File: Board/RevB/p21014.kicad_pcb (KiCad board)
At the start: 2 copper layers, 53.3 x 25.4 mm, 1 part

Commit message: Roughed out RevB PCB layout
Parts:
- added BT1: Battery_Cell, 0_MSD_FPs:AJS-Coin-Cell_1027-Digikey, B.Cu at (222.2, 60.2)
- added C1: 0.1uF, Capacitor_SMD:C_0603_1608Metric, F.Cu at (159.3, 44.6)
- added C2: 1uF, Capacitor_SMD:C_0603_1608Metric, F.Cu at (159.3, 42.1)
- added C3: 1uF, Capacitor_SMD:C_0603_1608Metric, F.Cu at (155.3, 44.6)
- added C4: 1uF, Capacitor_SMD:C_0603_1608Metric, F.Cu at (155.3, 42.1)
- added C5: 4.7uF_16V, Capacitor_Tantalum_SMD:CP_EIA-3216-18_Kemet-A, F.Cu at (156.2, 39.3)
- added D1: LED_RGB, 0_MSD_FPs:RGB_AJS, F.Cu at (128.6, 38.6)
- added D2: LED, LED_SMD:LED_1812_4532Metric, F.Cu at (118.2, 49.6)
- added J1: Conn_01x06_Male, 0_MSD_FPs:MSD_6_Pin, B.Cu at (193.7, 70.3)
- added J3: Conn_02x03_Counter_Clockwise, Connector_PinHeader_2.54mm:PinHeader_2x03_P2.54mm_Vertical, F.Cu at (214.0, 57.6)
- added J4: Conn_01x08_Female, 0_MSD_FPs:MSD_8_Pin, F.Cu at (179.8, 70.3)
- added J5: Conn_01x12_Female, 0_MSD_FPs:MSD_12_Pin, F.Cu at (190.0, 50.0)
- added J6: Conn_01x06_Female, 0_MSD_FPs:MSD_6_Pin, F.Cu at (205.2, 70.3)
- added MH1: MountingHole_2.5mm, MountingHole:MountingHole_2.5mm, F.Cu at (176.0, 51.3)
- added MH2: MountingHole_2.5mm, MountingHole:MountingHole_2.5mm, F.Cu at (224.3, 51.3)
- added MH3: MountingHole_2.5mm, MountingHole:MountingHole_2.5mm, F.Cu at (176.0, 69.0)
- added MH4: MountingHole_2.5mm, MountingHole:MountingHole_2.5mm, F.Cu at (224.3, 69.0)
- added R1: 350, Resistor_SMD:R_0603_1608Metric, F.Cu at (121.7, 41.4)
- added R2: 350, Resistor_SMD:R_0603_1608Metric, F.Cu at (125.7, 38.9)
- added R3: 350, Resistor_SMD:R_0603_1608Metric, F.Cu at (116.7, 53.3)
- added R4: 350, Resistor_SMD:R_0603_1608Metric, F.Cu at (121.7, 38.9)
- added R5: 10k, Resistor_SMD:R_0603_1608Metric, F.Cu at (123.7, 44.0)
- added R6: 10k, Resistor_SMD:R_0603_1608Metric, F.Cu at (125.7, 41.4)
- added R7: 10k, Resistor_SMD:R_0603_1608Metric, F.Cu at (109.8, 82.1)
- added SW1: SW_Push, 0_MSD_FPs:AJS-Switch_CFS-0102TA, B.Cu at (198.1, 31.8)
- added VR1: LM1117IMPX-5.0, LM1117IMPX-5:SOT230P700X180-4N, F.Cu at (148.5, 41.7)

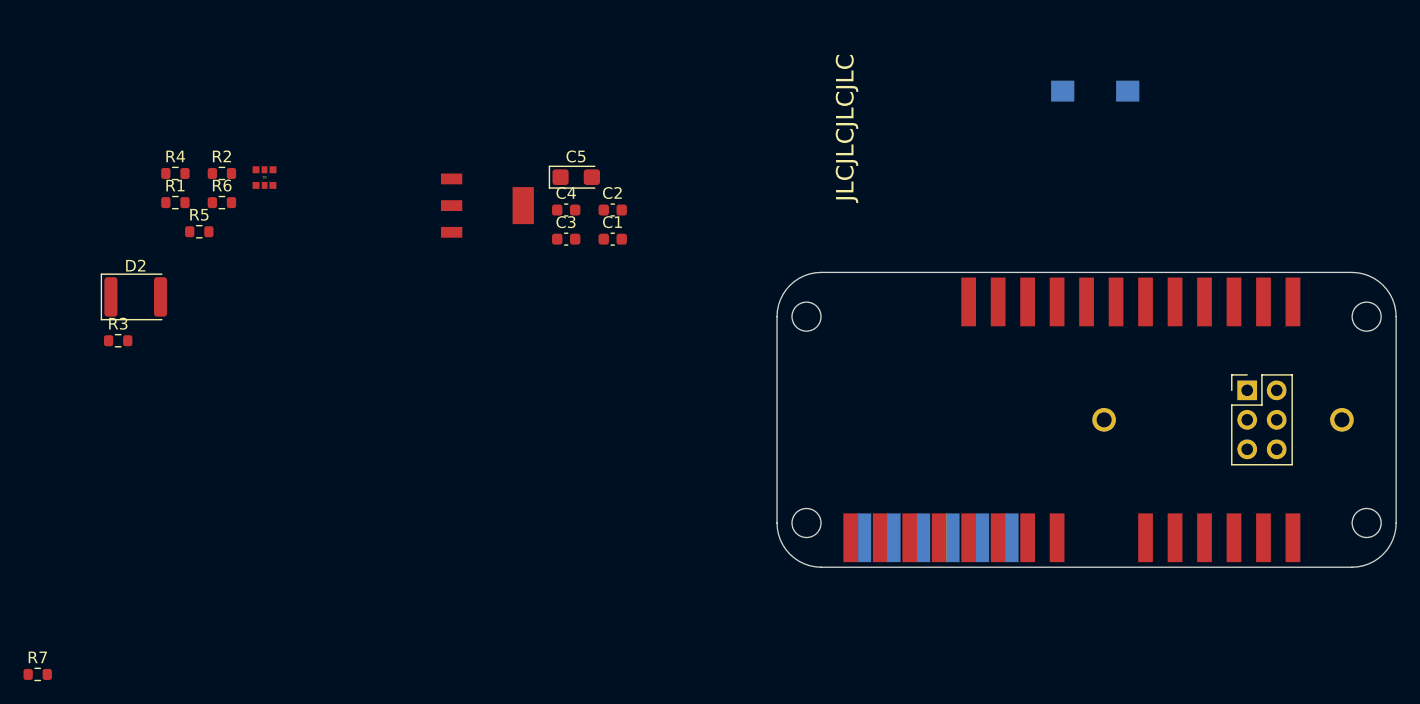
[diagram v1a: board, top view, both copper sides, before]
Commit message: Finished RevB Layout
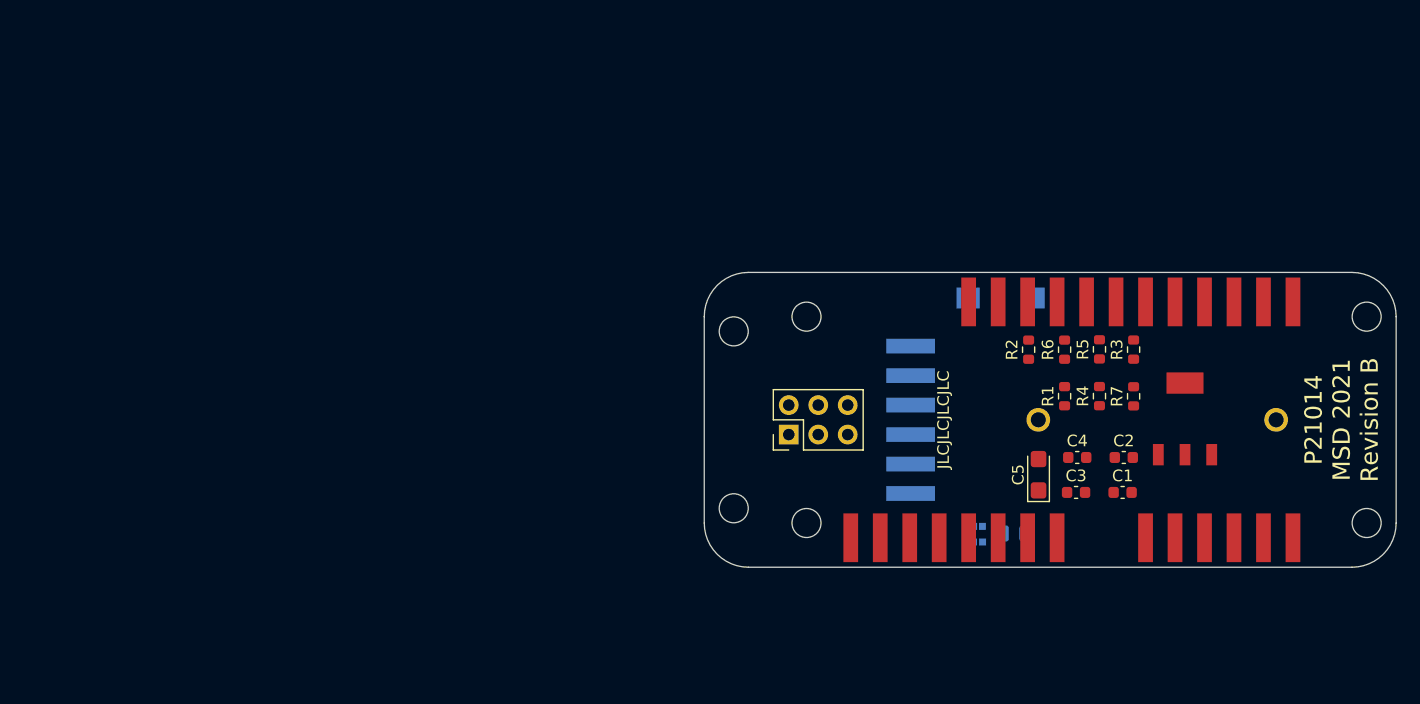
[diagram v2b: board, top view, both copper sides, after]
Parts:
- added MH5: MountingHole_2.5mm, MountingHole:MountingHole_2.5mm, F.Cu at (169.8, 67.8)
- added MH6: MountingHole_2.5mm, MountingHole:MountingHole_2.5mm, F.Cu at (169.8, 52.5)
- D1: moved to B.Cu
- D2: footprint LED_SMD:LED_1812_4532Metric -> 0_MSD_FPs:LED_0805_2012Metric; moved to B.Cu
- moved R7 97.4 mm to (204.2, 58.1), turned to 90 degrees
- moved R3 87.5 mm to (204.2, 54.1), turned to 90 degrees
- moved R4 81.9 mm to (201.3, 58.1), turned to 90 degrees
- moved R1 78.4 mm to (198.3, 58.1), turned to 90 degrees
- moved D2 78.4 mm to (193.9, 70.0)
- moved R5 78.2 mm to (201.3, 54.1), turned to 90 degrees
- moved R6 73.7 mm to (198.3, 54.1), turned to 90 degrees
- moved R2 71.1 mm to (195.2, 54.1), turned to 90 degrees
- moved D1 69.0 mm to (189.7, 70.7)
- moved VR1 62.8 mm to (208.6, 60.1), turned to 90 degrees
- moved C1 49.1 mm to (203.3, 66.4)
- moved C3 49.1 mm to (199.3, 66.4)
- moved C2 48.9 mm to (203.4, 63.4)
- moved C4 48.9 mm to (199.4, 63.4)
- moved C5 47.4 mm to (196.0, 64.9), turned to 90 degrees
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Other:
- board size 53.3 x 25.4 mm -> 59.6 x 25.4 mm
- board text added: "2 * CR2330 Batteries"
- board text added: "P21014 MSD 2021 Revision B"
- board text removed: "2*CR2330 Batteries"
- board text removed: "P21014 MSD 2021"

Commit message: Auto-routed RevB
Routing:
- net GNDREF: track 0.00 -> 109.8 mm, vias 0 -> 2
- net +5V: track 0.00 -> 67.1 mm, vias 0 -> 1
- net /RST: track 0.00 -> 57.9 mm, vias 0 -> 2
- net /SCL: track 0.00 -> 52.5 mm, vias 0 -> 2
- net Net-(J3-Pad6): track 0.00 -> 48.4 mm, vias 0 -> 1
- net Net-(J3-Pad1): track 0.00 -> 43.9 mm, vias 0 -> 1
- net /SDA: track 0.00 -> 42.4 mm, vias 0 -> 1
- net Net-(J3-Pad2): track 0.00 -> 40.6 mm
- net Net-(D1-Pad2): track 0.00 -> 37.0 mm, vias 0 -> 1
- net Net-(J3-Pad3): track 0.00 -> 34.9 mm, vias 0 -> 1
- net +BATT: track 0.00 -> 30.7 mm, vias 0 -> 1
- net Net-(J3-Pad4): track 0.00 -> 21.9 mm
- net Net-(D1-Pad3): track 0.00 -> 20.5 mm, vias 0 -> 1
- net Net-(D1-Pad1): track 0.00 -> 17.0 mm, vias 0 -> 1
- net Net-(D2-Pad2): track 0.00 -> 16.0 mm, vias 0 -> 1
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
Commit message: Created RevB Gerber Files
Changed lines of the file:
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@@
       (drillshape 0)
       (scaleselection 1)
-      (outputdirectory "../##Gerber/RevA/"))
+      (outputdirectory "../##Gerber/RevB/"))
   )
   (net 0 "")
@@
       (effects (font (size 0.8 0.8) (thickness 0.12)))
     )
-    (pad 1 smd roundrect (at -1.35 0 90) (size 1.4 1.35) (layers F.Cu F.Paste F.Mask) (roundrect_rratio 0.185185)
+    (pad 1 smd roundrect (at -1.35 0 90) (size 1.4 1.35) (layers F.Cu F.Paste F.Mask) (roundrect_rratio 0.1851844444444445)
       (net 4 +5V))
-    (pad 2 smd roundrect (at 1.35 0 90) (size 1.4 1.35) (layers F.Cu F.Paste F.Mask) (roundrect_rratio 0.185185)
+    (pad 2 smd roundrect (at 1.35 0 90) (size 1.4 1.35) (layers F.Cu F.Paste F.Mask) (roundrect_rratio 0.1851844444444445)
       (net 1 GNDREF))
     (model ${KISYS3DMOD}/Capacitor_Tantalum_SMD.3dshapes/CP_EIA-3216-18_Kemet-A.wrl
